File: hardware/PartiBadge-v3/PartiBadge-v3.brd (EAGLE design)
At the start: 118.9 x 117.7 mm, 26 parts, among them J1 I2C, J2 Supply

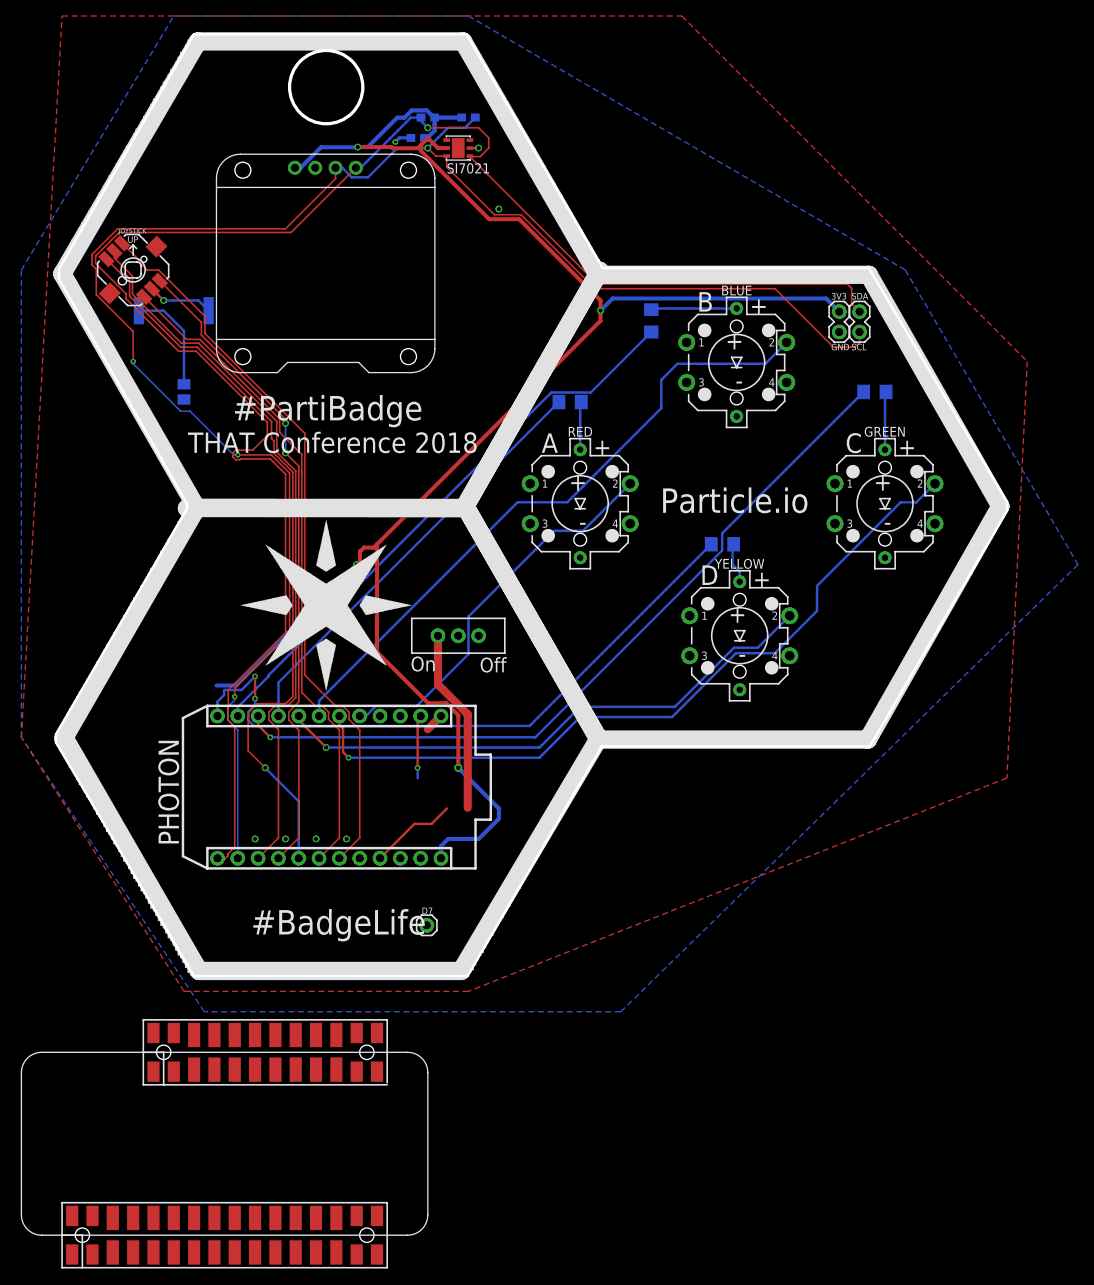
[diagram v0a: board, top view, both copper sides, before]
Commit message: added Xenon-based v3 design
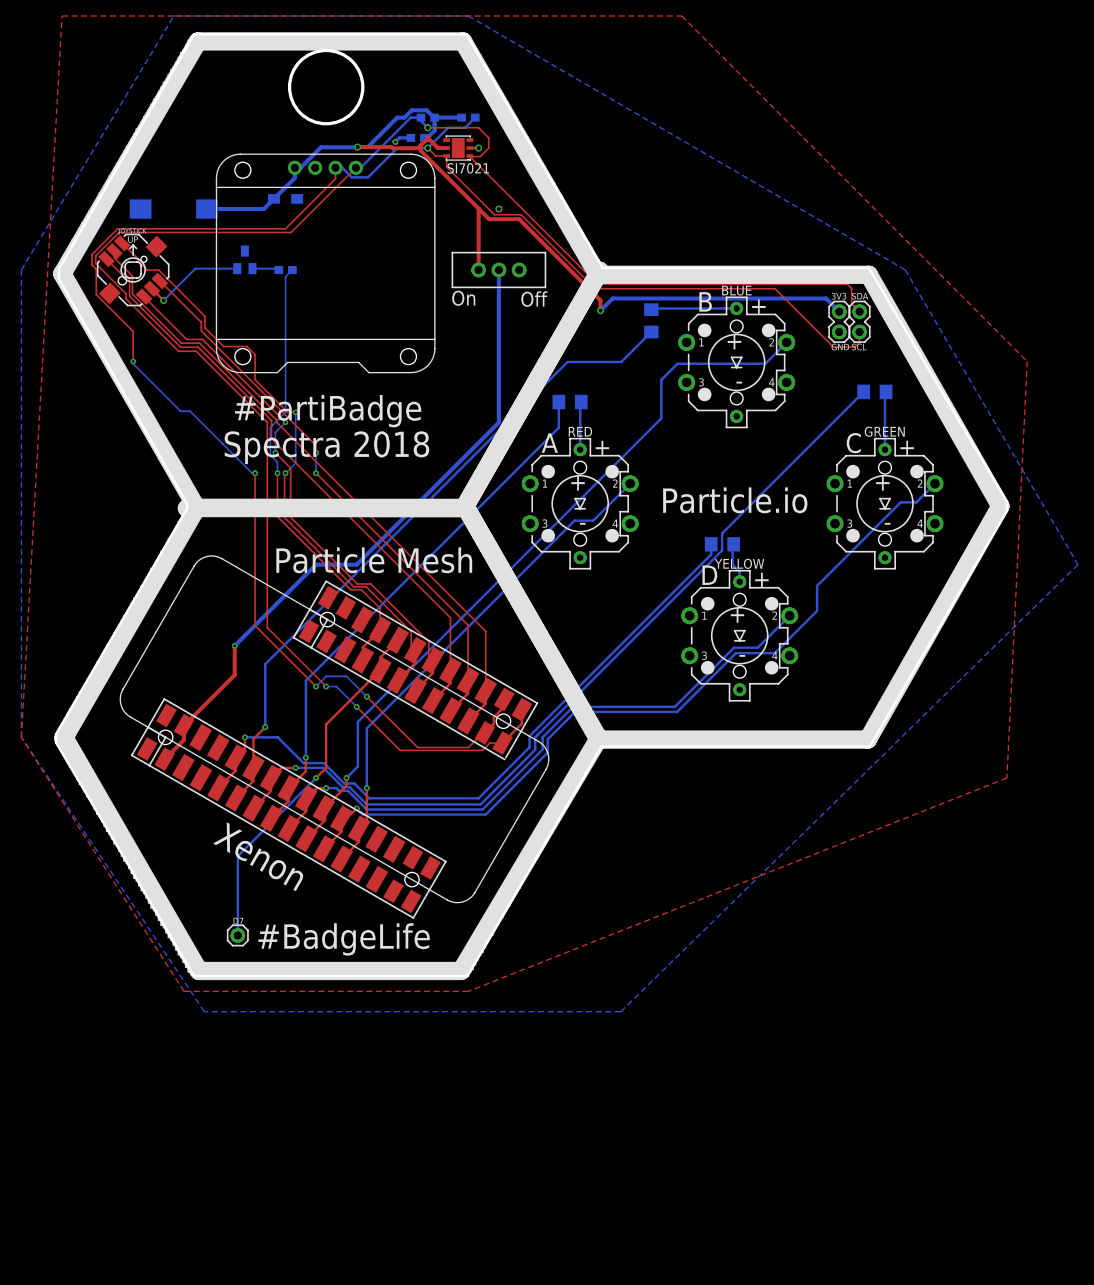
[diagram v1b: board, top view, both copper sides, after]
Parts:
- removed PHOTON: PHOTON_WITH_HEADERS, Particle-Devices:PHOTON
- removed PIEZO: PKMCS0909E4000-R1, PKMCS0909E4000-R1:XDCR_PKMCS0909E4000-R1
- removed R7: 200, rcl:M0805
- removed U$1: (no value), particle-spark:SPARK-LOGO
- added D1: (no value), diode:SOD323-W
- added LS1: SMT-1127-S-R, SMT-1127-S-R:XDCR_SMT-1127-S-R
- added R8: 180, SparkFun-Resistors:0603
- added T1: BC850, transistor:SOT23
- moved MS1 67.0 mm to (11.4, 36.8), turned to 330 degrees
- moved S5 46.0 mm to (59.7, 91.4)
- moved D7 23.7 mm to (27.1, 8.26)
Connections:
- removed net 5V: PHOTON.1
- removed net N$13: PIEZO.1, R7.1
- removed net N$2: MS1.15, MS1.15', R7.2
- removed net ON: S5.1
- removed net VBAT: PHOTON.22
- new net 3V3: MS1.2, MS1.2', S5.2
- new net N$3: MS1.25, MS1.25', R8.2
- new net N$5: R8.1, T1.1
- net +3V3: now also D1.C, LS1.1, S5.1; no longer PHOTON.24
- net BUTTON_B: now also MS1.10, MS1.10'; no longer PHOTON.7
- net BUTTON_G: now also MS1.11, MS1.11'; no longer PHOTON.6
- net BUTTON_R: now also MS1.12, MS1.12'; no longer PHOTON.5
- net BUTTON_Y: now also MS1.9, MS1.9'; no longer PHOTON.8
- net CENT: now also MS1.19, MS1.19'; no longer PHOTON.15
- net DOWN: now also MS1.22, MS1.22'; no longer PHOTON.18
- net GND: now also D1.A, LS1.2, T1.2, T1.3; no longer PHOTON.2, PHOTON.21, PIEZO.2
- net LED_B: now also MS1.6, MS1.6'; no longer PHOTON.11
- net LED_G: now also MS1.7, MS1.7'; no longer PHOTON.10
- net LED_R: now also MS1.8, MS1.8'; no longer PHOTON.9
- net LED_Y: now also MS1.5, MS1.5'; no longer PHOTON.12
- net LEFT: now also MS1.21, MS1.21'; no longer PHOTON.17
- net RIGHT: now also MS1.20, MS1.20'; no longer PHOTON.16
- net SCL: now also MS1.18, MS1.18'; no longer PHOTON.14
- net SDA: now also MS1.17, MS1.17'; no longer PHOTON.13
- net UP: now also MS1.23, MS1.23'; no longer PHOTON.19
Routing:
- net +3V3: track 224.6 -> 124.7 mm, vias 4 -> 2
- net 3V3: track 0.00 -> 81.4 mm, vias 0 -> 1
- net N$3: track 0.00 -> 57.3 mm, vias 0 -> 1
- net N$1: track 0.00 -> 45.2 mm, vias 0 -> 1
- net ON: track 23.0 -> 0.00 mm
- net LEFT: track 93.1 -> 75.4 mm, vias 1 -> 0
- net UP: track 91.6 -> 75.9 mm, vias 0 -> 2
- net BUTTON_R: track 48.6 -> 63.2 mm, vias 0 -> 1
- net DOWN: track 82.9 -> 68.3 mm, vias 0 -> 2
- net GND: track 30.3 -> 16.2 mm, vias 9 -> 4
- net N$13: track 13.3 -> 0.00 mm
- net LED_R: track 53.8 -> 66.9 mm, vias 0 -> 1
- net BUTTON_B: track 81.0 -> 93.6 mm, vias 0 -> 1
- net LED_B: track 72.3 -> 83.7 mm, vias 0 -> 1
- net RIGHT: track 81.4 -> 70.6 mm
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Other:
- board text added: "Particle Mesh"
- board text added: "Spectra 2018"
- board text added: "Xenon"
- board text removed: "THAT Conference 2018"

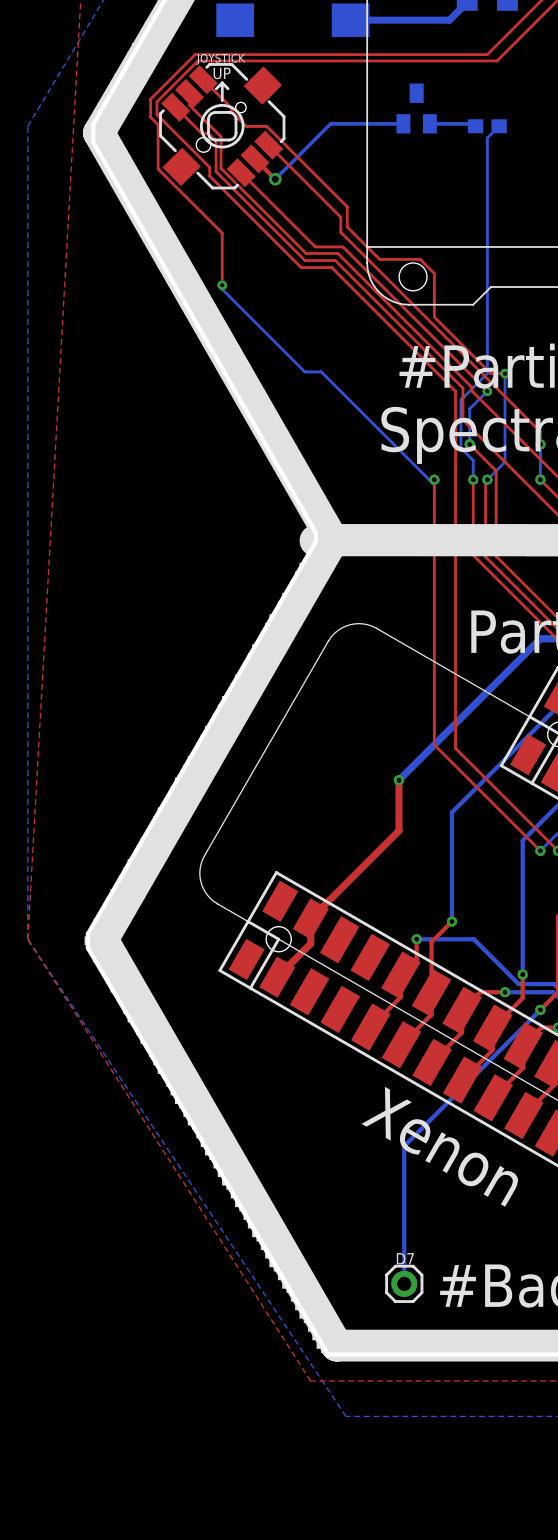
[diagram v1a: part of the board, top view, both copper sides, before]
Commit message: swapped out npn transistor
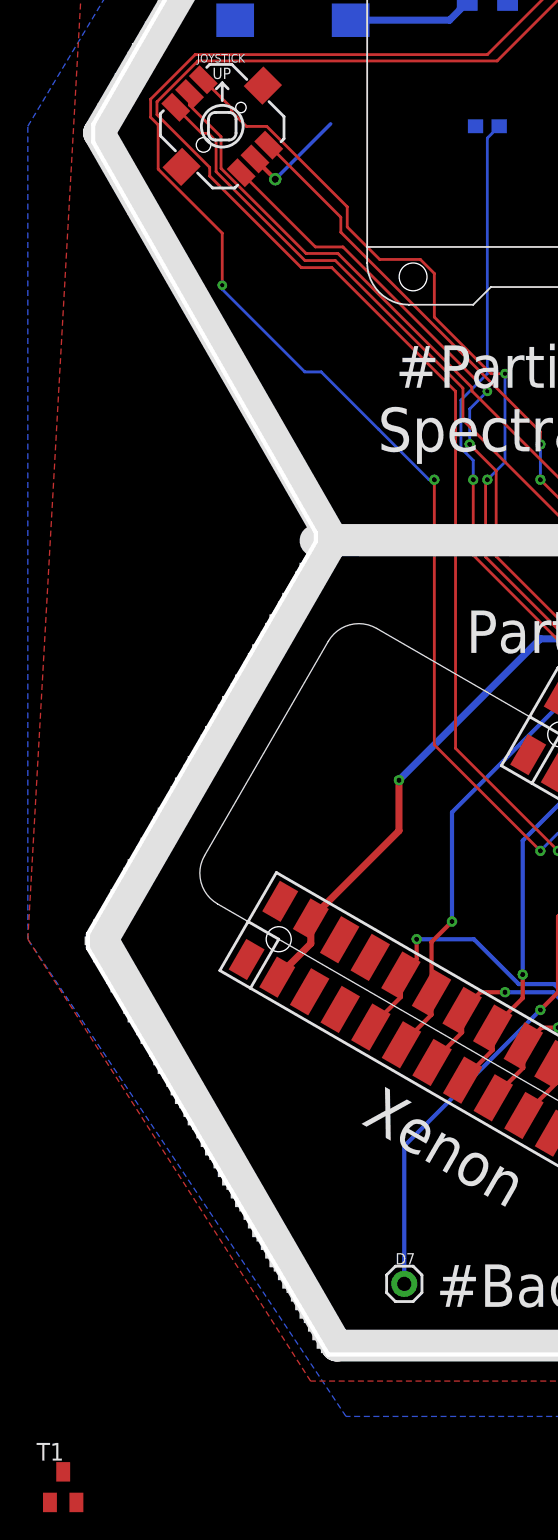
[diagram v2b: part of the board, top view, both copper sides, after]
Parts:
- R8: value 180 -> 1k
- T1: value BC850 -> MMBT4401-7-F; device transistor:SOT23 -> transistor:SOT23-BEC
- moved T1 102.3 mm to (2.54, -6.35), flipped to the top
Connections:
- net GND: now also T1.C, T1.E; no longer T1.2, T1.3
- net N$5: now also T1.B; no longer T1.1
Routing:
- net GND: track 16.2 -> 10.9 mm
- net N$5: track 3.35 -> 0.24 mm
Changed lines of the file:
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@@
 </element>
 <element name="MS1" library="Particle-Mesh" package="FEATHERWING_SMT2" value="PARTICLE_MESH_SMTDUAL" x="11.43" y="36.83" rot="R330"/>
-<element name="T1" library="transistor" library_urn="urn:adsk.eagle:library:402" package="SOT23" package3d_urn="urn:adsk.eagle:package:29904/2" value="BC850" x="27.94" y="92.71" rot="MR0"/>
 <element name="D1" library="diode" library_urn="urn:adsk.eagle:library:210" package="SOD323-W" package3d_urn="urn:adsk.eagle:package:43418/1" value="" x="33.02" y="100.33" rot="MR180"/>
-<element name="R8" library="SparkFun-Resistors" library_urn="urn:adsk.eagle:library:532" package="0603" package3d_urn="urn:adsk.eagle:package:39650/1" value="180" x="33.02" y="91.44" rot="MR180">
+<element name="R8" library="SparkFun-Resistors" library_urn="urn:adsk.eagle:library:532" package="0603" package3d_urn="urn:adsk.eagle:package:39650/1" value="1k" x="33.02" y="91.44" rot="MR180">
 <attribute name="PROD_ID" value="RES-00824" x="33.02" y="91.44" size="1.778" layer="28" rot="MR180" display="off"/>
 </element>
@@
 <attribute name="PACKAGE" value=" PUI" x="19.05" y="99.06" size="1.778" layer="28" rot="MR0" display="off"/>
 </element>
+<element name="T1" library="transistor" library_urn="urn:adsk.eagle:library:402" package="SOT23-BEC" package3d_urn="urn:adsk.eagle:package:28748/2" value="MMBT4401-7-F" x="2.54" y="-6.35"/>
 </elements>
 <signals>
@@
 <contactref element="MS1" pad="4'"/>
 <contactref element="MS1" pad="4"/>
-<contactref element="T1" pad="2"/>
-<contactref element="T1" pad="3"/>
 <contactref element="D1" pad="A"/>
 <contactref element="LS1" pad="2"/>
 <wire x1="17.78" y1="87.63" x2="21.76" y2="91.61" width="0.254" layer="16"/>
-<wire x1="21.76" y1="91.61" x2="26.99" y2="91.61" width="0.254" layer="16"/>
+<contactref element="T1" pad="E"/>
+<contactref element="T1" pad="C"/>
+<wire x1="95.658" y1="77.383" x2="102.235" y2="83.693" width="0" layer="19" extent="1-1"/>
+<wire x1="89.408" y1="73.133" x2="95.658" y2="77.383" width="0" layer="19" extent="1-1"/>
+<wire x1="76.1" y1="59.73" x2="89.408" y2="73.133" width="0" layer="19" extent="1-1"/>
+<wire x1="69.85" y1="55.48" x2="76.1" y2="59.73" width="0" layer="19" extent="1-1"/>
+<wire x1="89.789" y1="38.97" x2="76.1" y2="59.73" width="0" layer="19" extent="1-1"/>
+<wire x1="96.039" y1="43.22" x2="89.789" y2="38.97" width="0" layer="19" extent="1-1"/>
+<wire x1="107.95" y1="55.48" x2="96.039" y2="43.22" width="0" layer="19" extent="1-1"/>
+<wire x1="114.2" y1="59.73" x2="107.95" y2="55.48" width="0" layer="19" extent="1-1"/>
+<wire x1="59.69" y1="99.06" x2="89.408" y2="73.133" width="0" layer="19" extent="1-1"/>
+<wire x1="57.15" y1="106.68" x2="59.69" y2="99.06" width="0" layer="19" extent="1-1"/>
+<wire x1="48.68" y1="107.95" x2="56.06" y2="106.68" width="0" layer="19" extent="1-16"/>
+<wire x1="36.724" y1="104.213" x2="46.736" y2="107.442" width="0" layer="19" extent="16-16"/>
+<wire x1="34.47" y1="100.33" x2="36.724" y2="104.213" width="0" layer="19" extent="16-16"/>
+<wire x1="21.76" y1="91.61" x2="34.47" y2="100.33" width="0" layer="19" extent="16-16"/>
+<wire x1="14.9" y1="99.06" x2="16.321128125" y2="89.08886875" width="0" layer="19" extent="1-16"/>
+<wire x1="24.607871875" y1="31.714746875" x2="69.85" y2="55.48" width="0" layer="19" extent="1-1"/>
+<wire x1="22.448871875" y1="27.97525" x2="24.607871875" y2="31.714746875" width="0" layer="19" extent="1-1"/>
+<wire x1="2.54" y1="-5.25" x2="22.448871875" y2="27.97525" width="0" layer="19" extent="1-1"/>
+<wire x1="3.49" y1="-7.45" x2="2.54" y2="-5.25" width="0" layer="19" extent="1-1"/>
 </signal>
 <signal name="+3V3">
@@
 <signal name="N$5">
 <contactref element="R8" pad="1"/>
-<contactref element="T1" pad="1"/>
-<wire x1="28.89" y1="91.61" x2="32" y2="91.61" width="0.254" layer="16"/>
 <wire x1="32" y1="91.61" x2="32.17" y2="91.44" width="0.254" layer="16"/>
+<contactref element="T1" pad="B"/>
+<wire x1="1.59" y1="-7.45" x2="32.17" y2="91.44" width="0" layer="19" extent="1-16"/>
 </signal>
 </signals>
